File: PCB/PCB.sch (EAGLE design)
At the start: 216 parts, among them J3 Boot, Q1 FS8205A, U1 ESP32-S3HOLE

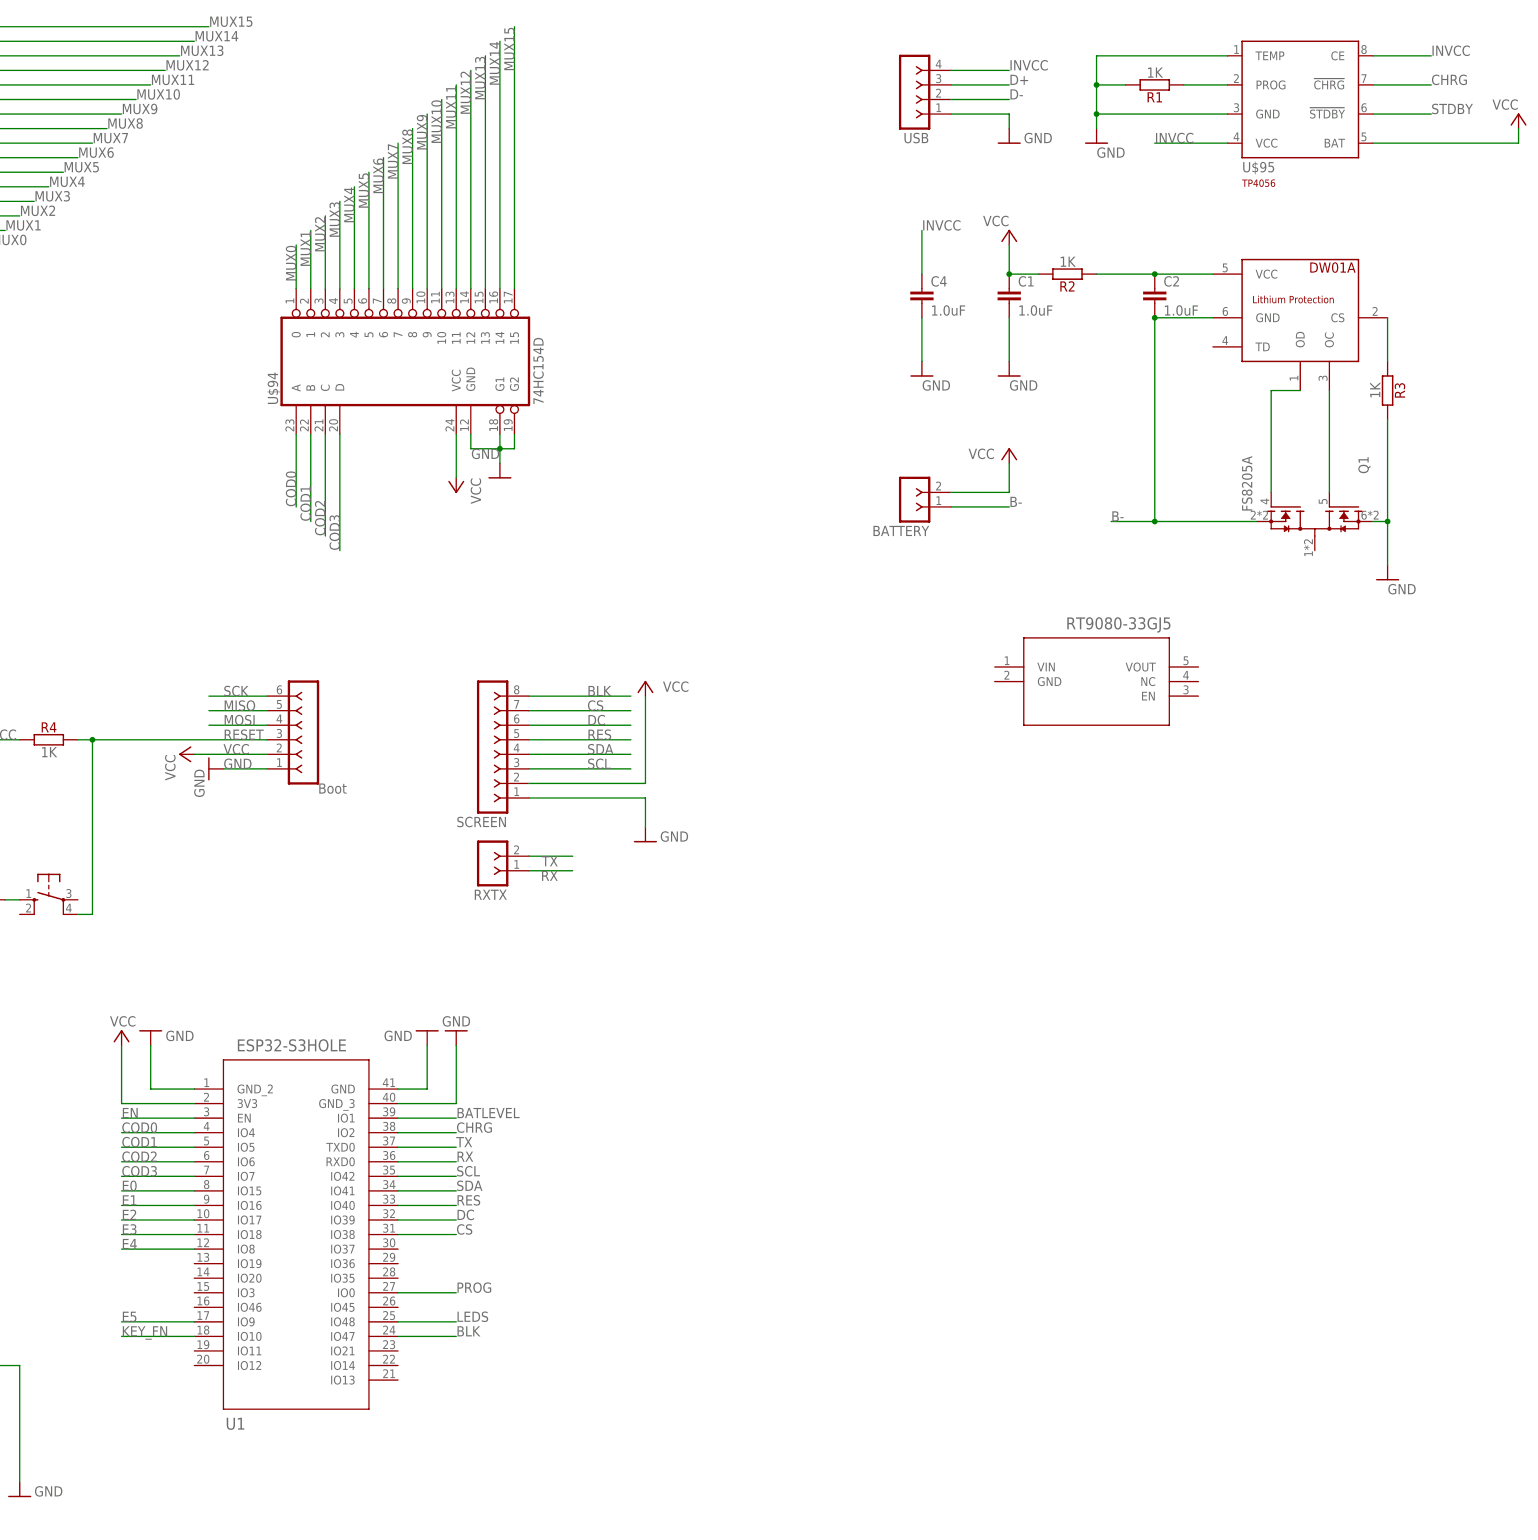
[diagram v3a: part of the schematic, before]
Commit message: Finished the power circuit for the keyboard
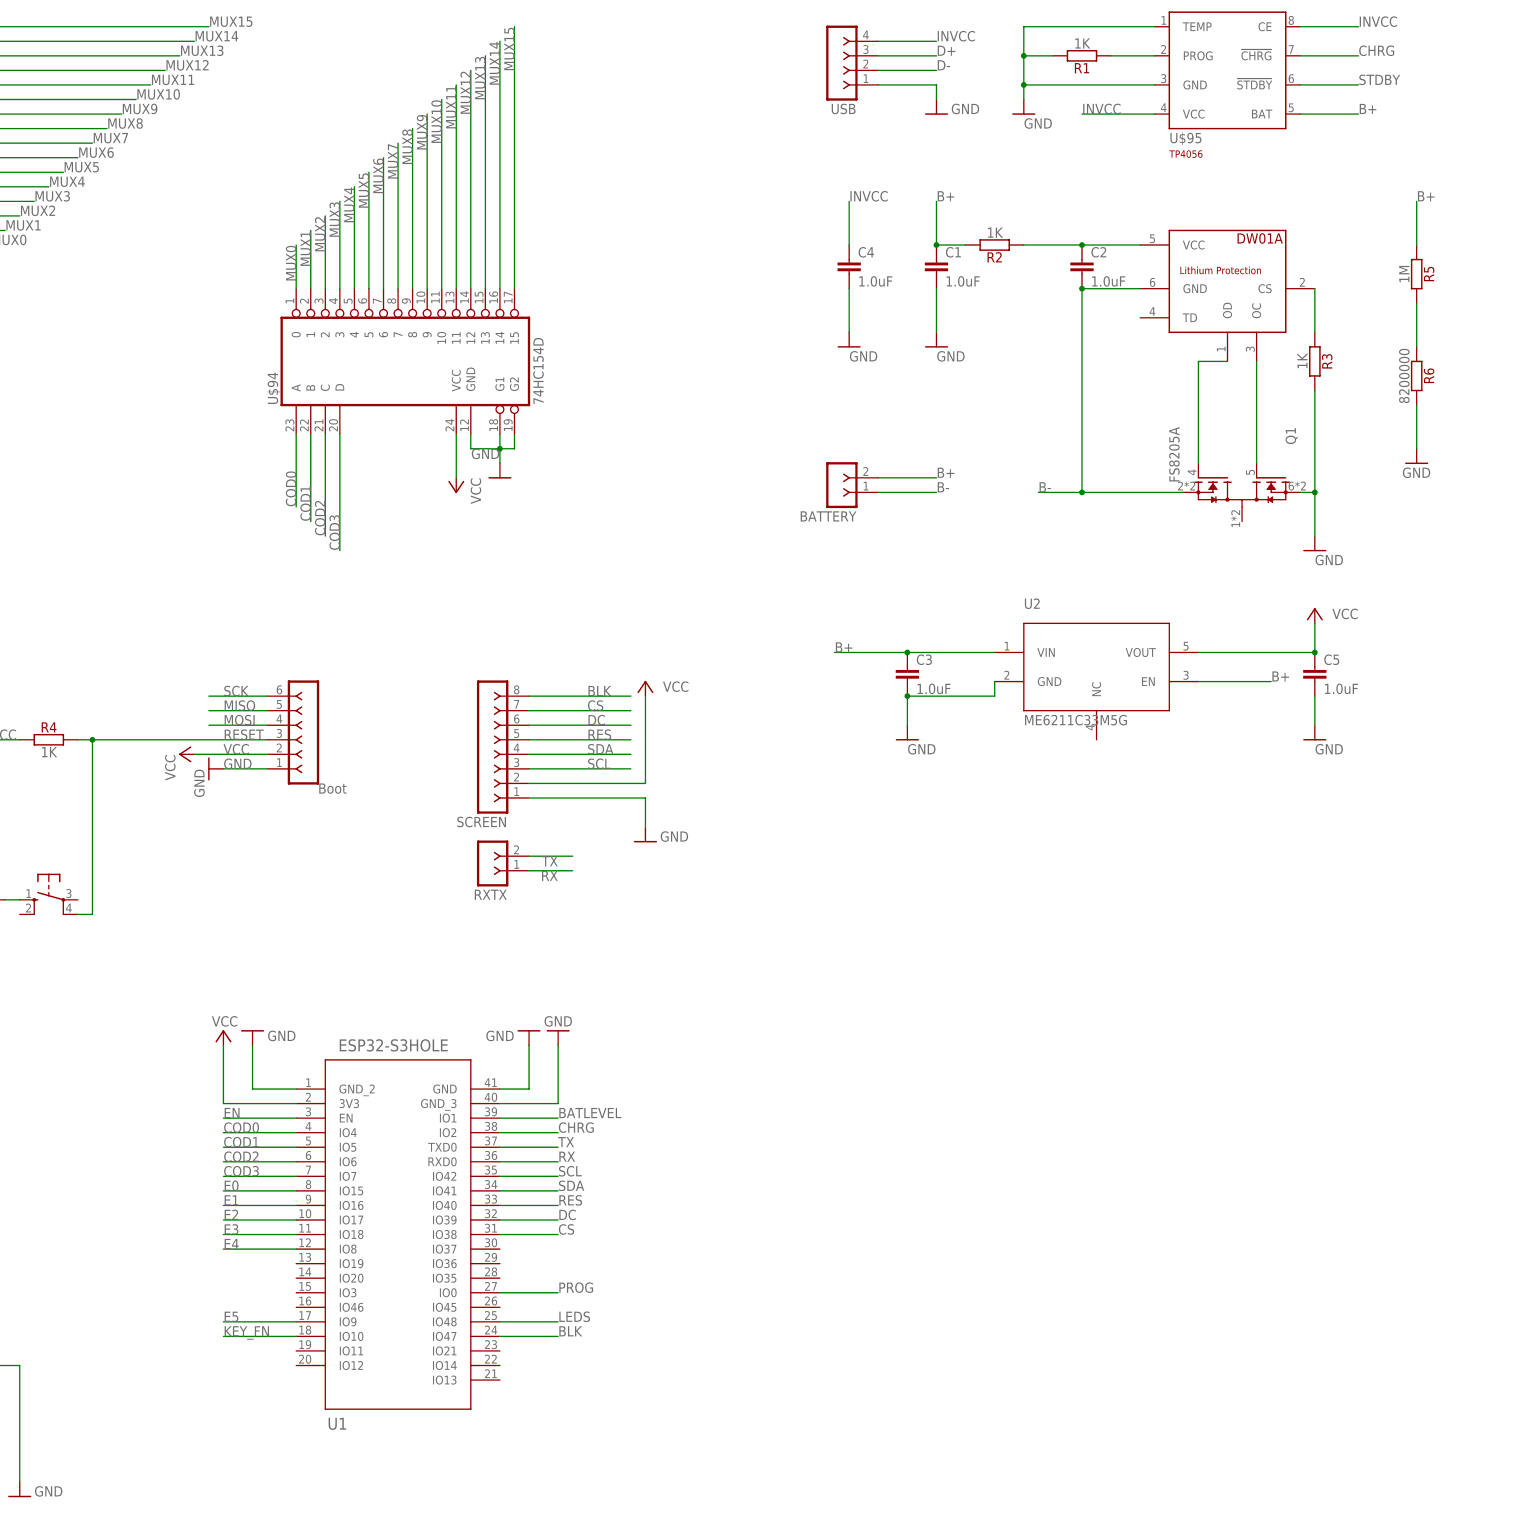
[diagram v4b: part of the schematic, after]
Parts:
- removed REGULATOR: RT9080-33GJ5, RT9080:RT9080-33GJ5
- added C3, C5: 1.0uF, SparkFun-Capacitors:1.0UF-1206-50V-10%
- added R5: 1M, resistors:1K
- added R6: 8200000, resistors:1K
- added U2: ME6211C33M5G, ME6211:ME6211C33M5G
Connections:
- new net B+: BATTERY.2, C1.1, C3.1, R2.2, R5.1, U$95.BAT, U2.EN, U2.VIN
- new net N$35: R5.2, R6.1
- net GND: now also C3.2, C5.2, R6.2, U2.GND
- net VCC: now also C5.1, U2.VOUT; no longer BATTERY.2, C1.1, R2.2, U$95.BAT
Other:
- moved on the sheet: BATTERY, C1, C2, C4, Q1, R1, R2, R3, U$95, U1, USB

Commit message: Finished .sch
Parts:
- removed J3: Boot, con-headers-jp:F-1X06-SIP-100-32
- removed RXTX: F-1X02-SIP-100-40, con-headers-jp:F-1X02-SIP-100-40
- added BOOT: BOOT, con-headers-jp:F-1X04-SIP-100-32
- added BUTTON1: 1, switch-omron:10-XX
- added R7: 1K, resistors:1K
- added U$67: WS2812B5050, Led-WS2812B:WS2812B5050
- BUTTON: value (none) -> 1
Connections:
- removed net MISO: J3.5
- removed net MOSI: J3.4
- removed net RESET: BUTTON.P1, J3.3, R4.2
- removed net SCK: J3.6
- new net N$79: U$67.LED_VDD
- net BATLEVEL: now also R5.2, R6.1
- net D+: now also U1.IO20
- net D-: now also U1.IO19
- net EN: now also BUTTON1.P1, R7.2
- net GND: now also BOOT.1, BUTTON1.S; no longer J3.1
- net LEDS: now also U$67.LED_DI
- net N$35: now also U$67.LED_GND; no longer R5.2, R6.1
- net PROG: now also BUTTON.P1, R4.2
- net RX: now also BOOT.4; no longer RXTX.1
- net STDBY: now also U1.IO21
- net TX: now also BOOT.3; no longer RXTX.2
- net VCC: now also BOOT.2, R7.1; no longer J3.2
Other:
- moved on the sheet: R4, R5

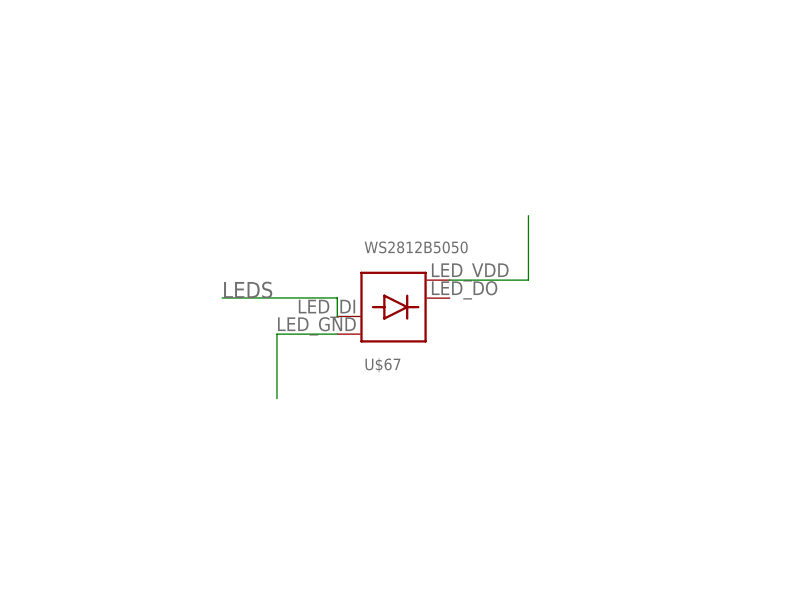
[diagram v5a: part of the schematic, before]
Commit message: Added new holes and changed the pcb layaout to fit the usb connector
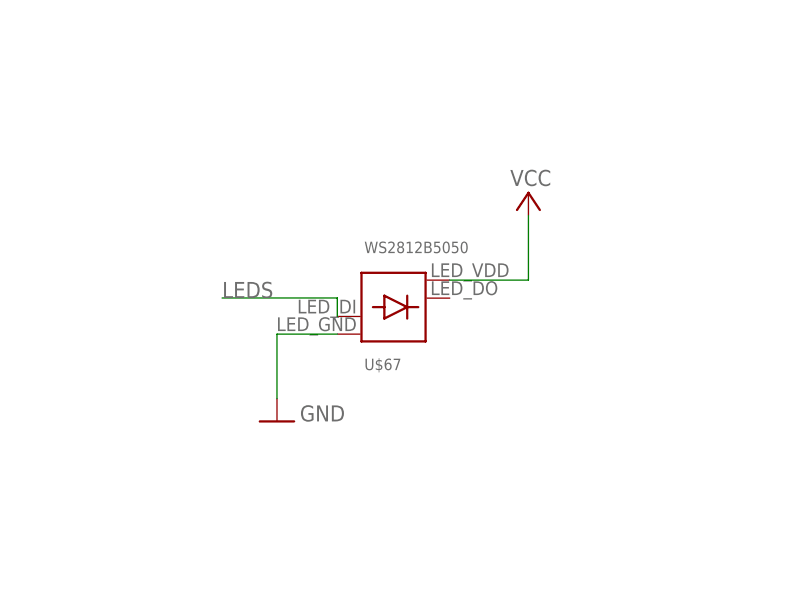
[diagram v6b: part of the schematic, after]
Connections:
- removed net N$35: U$67.LED_GND
- removed net N$79: U$67.LED_VDD
- net GND: now also U$67.LED_GND
- net VCC: now also U$67.LED_VDD
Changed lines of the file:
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@@
 <part name="GND12" library="supply1" library_urn="urn:adsk.eagle:library:371" deviceset="GND" device=""/>
 <part name="U$67" library="Led-WS2812B" deviceset="WS2812B5050" device=""/>
+<part name="GND18" library="supply1" library_urn="urn:adsk.eagle:library:371" deviceset="GND" device=""/>
+<part name="P+6" library="supply1" library_urn="urn:adsk.eagle:library:371" deviceset="VCC" device=""/>
 </parts>
 <sheets>
@@
 <attribute name="NAME" x="677.72" y="79.36" size="1.27" layer="95"/>
 </instance>
+<instance part="GND18" gate="1" x="668.02" y="73.66" smashed="yes">
+<attribute name="VALUE" x="670.56" y="73.66" size="1.778" layer="96"/>
+</instance>
+<instance part="P+6" gate="VCC" x="695.96" y="99.06" smashed="yes">
+<attribute name="VALUE" x="698.5" y="101.6" size="1.778" layer="96" rot="R180"/>
+</instance>
 </instances>
 <busses>
@@
 <pinref part="GND12" gate="1" pin="GND"/>
 </segment>
+<segment>
+<pinref part="U$67" gate="G$1" pin="LED_GND"/>
+<wire x1="674.72" y1="83.36" x2="668.02" y2="83.36" width="0.1524" layer="91"/>
+<wire x1="668.02" y1="83.36" x2="668.02" y2="76.2" width="0.1524" layer="91"/>
+<pinref part="GND18" gate="1" pin="GND"/>
+</segment>
 </net>
 <net name="E4" class="0">
@@
 <pinref part="P+3" gate="VCC" pin="VCC"/>
 </segment>
+<segment>
+<pinref part="U$67" gate="G$1" pin="LED_VDD"/>
+<wire x1="687.22" y1="89.36" x2="695.96" y2="89.36" width="0.1524" layer="91"/>
+<wire x1="695.96" y1="89.36" x2="695.96" y2="96.52" width="0.1524" layer="91"/>
+<pinref part="P+6" gate="VCC" pin="VCC"/>
+</segment>
 </net>
 <net name="COD0" class="0">
@@
 </segment>
 </net>
-<net name="N$35" class="0">
-<segment>
-<pinref part="U$67" gate="G$1" pin="LED_GND"/>
-<wire x1="674.72" y1="83.36" x2="668.02" y2="83.36" width="0.1524" layer="91"/>
-<wire x1="668.02" y1="83.36" x2="668.02" y2="76.2" width="0.1524" layer="91"/>
-</segment>
-</net>
-<net name="N$79" class="0">
-<segment>
-<pinref part="U$67" gate="G$1" pin="LED_VDD"/>
-<wire x1="687.22" y1="89.36" x2="695.96" y2="89.36" width="0.1524" layer="91"/>
-<wire x1="695.96" y1="89.36" x2="695.96" y2="96.52" width="0.1524" layer="91"/>
-</segment>
-</net>

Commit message: Finished PCB Board and Schematic
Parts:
- added U$100, U$101, U$102, U$103, U$104, U$105, U$97, U$98, U$99: WS2812B5050, Led-WS2812B:WS2812B5050
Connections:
- net N$31 renamed TPPROG
- net N$32 renamed DWCS
- net N$33 renamed DWOC
- net N$34 renamed DWOD
- net N$36 renamed DWVCC
- new net N$100: U$100.LED_DI, U$99.LED_DO
- new net N$101: U$100.LED_DO, U$101.LED_DI
- new net N$102: U$101.LED_DO, U$102.LED_DI
- new net N$103: U$102.LED_DO, U$103.LED_DI
- new net N$104: U$103.LED_DO, U$104.LED_DI
- new net N$105: U$104.LED_DO, U$105.LED_DI
- new net N$106: U$67.LED_DO, U$97.LED_DI
- new net N$35: U$97.LED_DO, U$98.LED_DI
- new net N$79: U$98.LED_DO, U$99.LED_DI
- net GND: now also U$100.LED_GND, U$101.LED_GND, U$102.LED_GND, U$103.LED_GND, U$104.LED_GND, U$105.LED_GND, U$97.LED_GND, U$98.LED_GND, U$99.LED_GND
- net VCC: now also U$100.LED_VDD, U$101.LED_VDD, U$102.LED_VDD, U$103.LED_VDD, U$104.LED_VDD, U$105.LED_VDD, U$97.LED_VDD, U$98.LED_VDD, U$99.LED_VDD
